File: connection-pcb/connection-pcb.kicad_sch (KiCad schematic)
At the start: 19 parts, among them J1 Conn_01x05, J2 Conn_01x05, J3 Conn_01x05, J4 Conn_01x05, J5 Conn_01x05, J6 Screw_Terminal_01x04, J7 Screw_Terminal_01x02, J8 Screw_Terminal_01x06, J9 DE9_Socket_MountingHoles, SW1 SW_DIP_x04

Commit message: Footprints and DRC (Connection PCB)
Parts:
- J1, J2, J3, J4, J5: footprint (none) -> Connector_Molex:Molex_SPOX_5267-05A_1x05_P2.50mm_Vertical
- J6: footprint (none) -> Exocet:Wurth_Term_Blk_4pos_Side_Entry_5mm
- J7: footprint (none) -> Exocet:Wurth_Term_Blk_2pos_Side_Entry_5mm
- J8: footprint (none) -> Exocet:Wurth_Term_Blk_6pos_Side_Entry_5mm
- J9: footprint (none) -> Connector_Dsub:DSUB-9_Socket_Horizontal_P2.77x2.84mm_EdgePinOffset7.70mm_Housed_MountingHolesOffset9.12mm
- R1, R2, R3: footprint (none) -> Resistor_THT:R_Axial_DIN0309_L9.0mm_D3.2mm_P12.70mm_Horizontal
- SW1: footprint (none) -> Button_Switch_THT:SW_DIP_SPSTx04_Slide_6.7x11.72mm_W7.62mm_P2.54mm_LowProfile
- TP1, TP2, TP3, TP4, TP5, TP6: footprint (none) -> TestPoint:TestPoint_Keystone_5005-5009_Compact
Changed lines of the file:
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@@
 			)
 		)
-		(property "Footprint" ""
+		(property "Footprint" "TestPoint:TestPoint_Keystone_5005-5009_Compact"
 			(at 205.74 24.13 0)
 			(effects
@@
 			)
 		)
-		(property "Footprint" ""
+		(property "Footprint" "TestPoint:TestPoint_Keystone_5005-5009_Compact"
 			(at 226.06 22.86 0)
 			(effects
@@
 			)
 		)
-		(property "Footprint" ""
+		(property "Footprint" "Connector_Molex:Molex_SPOX_5267-05A_1x05_P2.50mm_Vertical"
 			(at 21.59 31.75 0)
 			(effects
@@
 			)
 		)
-		(property "Footprint" ""
+		(property "Footprint" "TestPoint:TestPoint_Keystone_5005-5009_Compact"
 			(at 220.98 39.37 0)
 			(effects
@@
 			)
 		)
-		(property "Footprint" ""
+		(property "Footprint" "Resistor_THT:R_Axial_DIN0309_L9.0mm_D3.2mm_P12.70mm_Horizontal"
 			(at 198.12 80.518 90)
 			(effects
@@
 			)
 		)
-		(property "Footprint" ""
+		(property "Footprint" "Exocet:Wurth_Term_Blk_4pos_Side_Entry_5mm"
 			(at 160.02 30.48 0)
 			(effects
@@
 			)
 		)
-		(property "Footprint" ""
+		(property "Footprint" "Exocet:Wurth_Term_Blk_6pos_Side_Entry_5mm"
 			(at 93.98 71.12 0)
 			(effects
@@
 			)
 		)
-		(property "Footprint" ""
+		(property "Footprint" "Resistor_THT:R_Axial_DIN0309_L9.0mm_D3.2mm_P12.70mm_Horizontal"
 			(at 152.4 77.978 90)
 			(effects
@@
 			)
 		)
-		(property "Footprint" ""
+		(property "Footprint" "TestPoint:TestPoint_Keystone_5005-5009_Compact"
 			(at 195.58 38.1 0)
 			(effects
@@
 			)
 		)
-		(property "Footprint" ""
+		(property "Footprint" "TestPoint:TestPoint_Keystone_5005-5009_Compact"
 			(at 210.82 22.86 0)
 			(effects
@@
 			)
 		)
-		(property "Footprint" ""
+		(property "Footprint" "Connector_Molex:Molex_SPOX_5267-05A_1x05_P2.50mm_Vertical"
 			(at 123.19 31.75 0)
 			(effects
@@
 			)
 		)
-		(property "Footprint" ""
+		(property "Footprint" "Connector_Molex:Molex_SPOX_5267-05A_1x05_P2.50mm_Vertical"
 			(at 97.79 31.75 0)
 			(effects
@@
 			)
 		)
-		(property "Footprint" ""
+		(property "Footprint" "Button_Switch_THT:SW_DIP_SPSTx04_Slide_6.7x11.72mm_W7.62mm_P2.54mm_LowProfile"
 			(at 176.53 76.2 0)
 			(effects
@@
 			)
 		)
-		(property "Footprint" ""
+		(property "Footprint" "Connector_Molex:Molex_SPOX_5267-05A_1x05_P2.50mm_Vertical"
 			(at 72.39 31.75 0)
 			(effects
@@
 			)
 		)
-		(property "Footprint" ""
+		(property "Footprint" "Connector_Molex:Molex_SPOX_5267-05A_1x05_P2.50mm_Vertical"
 			(at 46.99 31.75 0)
 			(effects
@@
 			)
 		)
-		(property "Footprint" ""
+		(property "Footprint" "Connector_Dsub:DSUB-9_Socket_Horizontal_P2.77x2.84mm_EdgePinOffset7.70mm_Housed_MountingHolesOffset9.12mm"
 			(at 48.26 71.12 0)
 			(effects
@@
 			)
 		)
-		(property "Footprint" ""
+		(property "Footprint" "Exocet:Wurth_Term_Blk_2pos_Side_Entry_5mm"
 			(at 264.16 30.48 0)
 			(effects
@@
 			)
 		)
-		(property "Footprint" ""
+		(property "Footprint" "Resistor_THT:R_Axial_DIN0309_L9.0mm_D3.2mm_P12.70mm_Horizontal"
 			(at 106.172 82.55 90)
 			(effects
@@
 			)
 		)
-		(property "Footprint" ""
+		(property "Footprint" "TestPoint:TestPoint_Keystone_5005-5009_Compact"
 			(at 236.22 39.37 0)
 			(effects

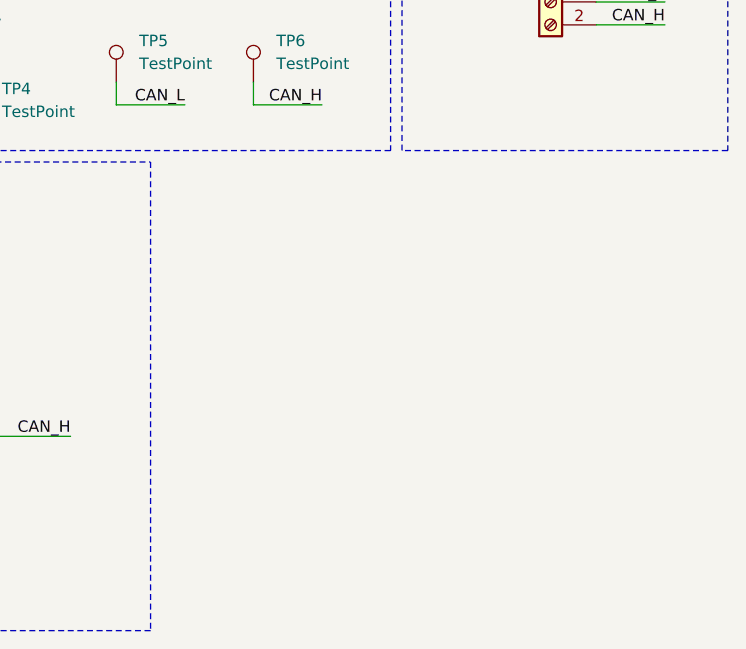
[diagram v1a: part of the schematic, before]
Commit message: Add mounting holes
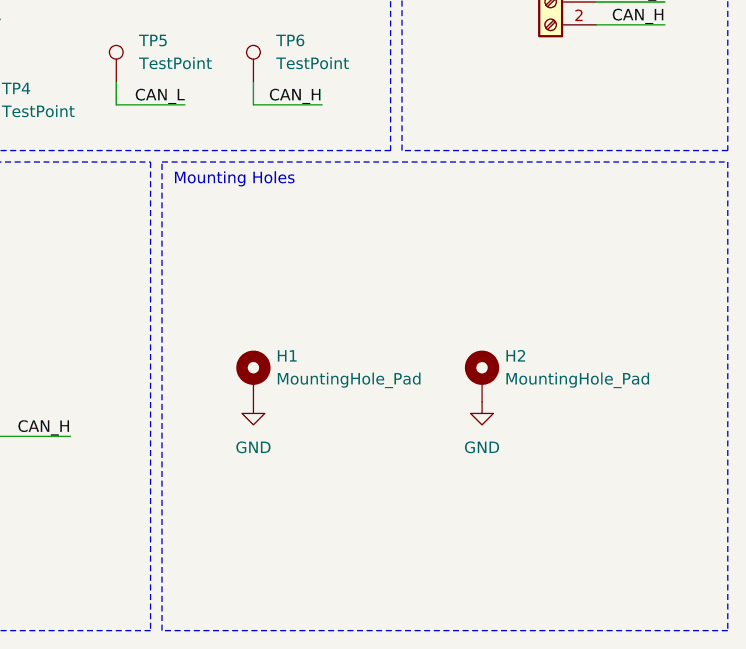
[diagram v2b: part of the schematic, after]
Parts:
- added H1, H2: MountingHole_Pad, MountingHole:MountingHole_2.7mm_M2.5_ISO7380_Pad, symbol Mechanical:MountingHole_Pad
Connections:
- net GND: now also H1.1, H2.1
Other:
- note added: "Mounting Holes"
